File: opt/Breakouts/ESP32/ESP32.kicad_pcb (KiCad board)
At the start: 2 copper layers, 23.4 x 25.9 mm, 3 parts, among them J1 LEFT, J2 RIGHT, U2 ESP32-S3-MINI-1

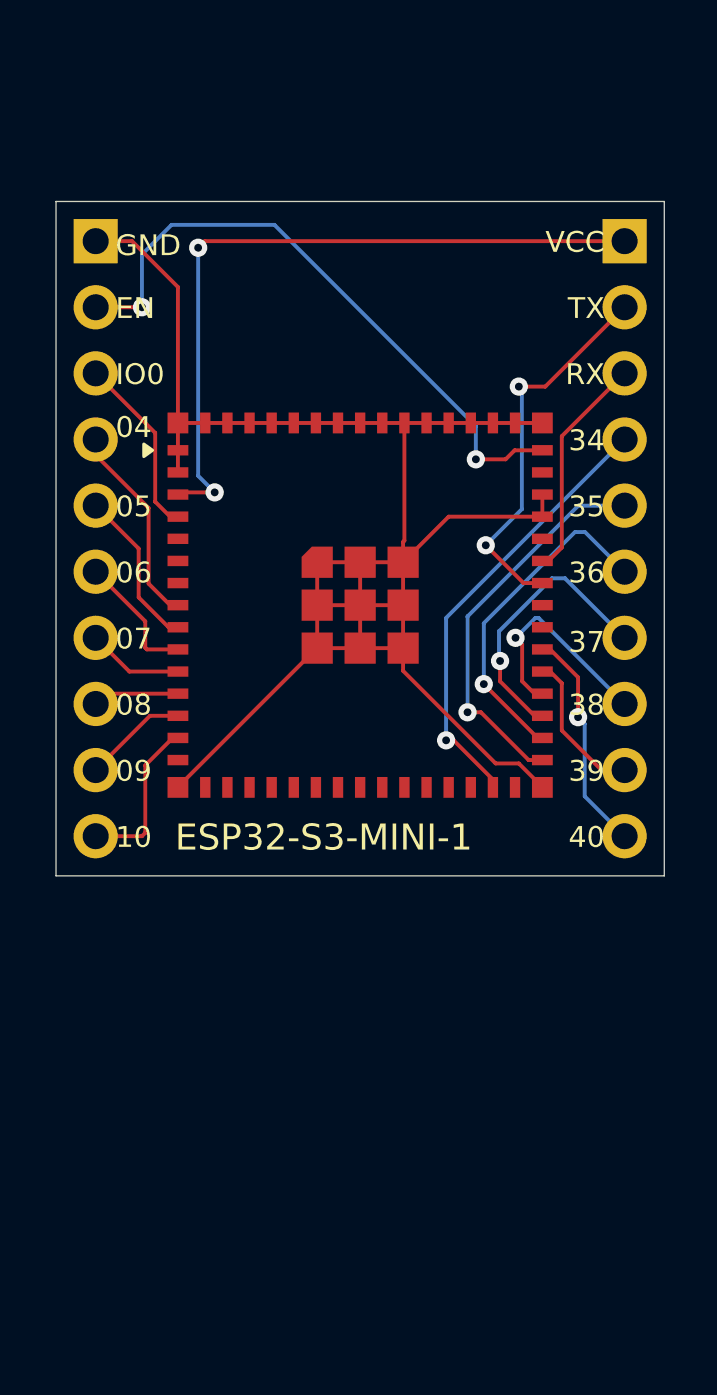
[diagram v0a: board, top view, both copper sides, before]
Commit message: breakouts: Merge ESP32 and PT8211 pcbs
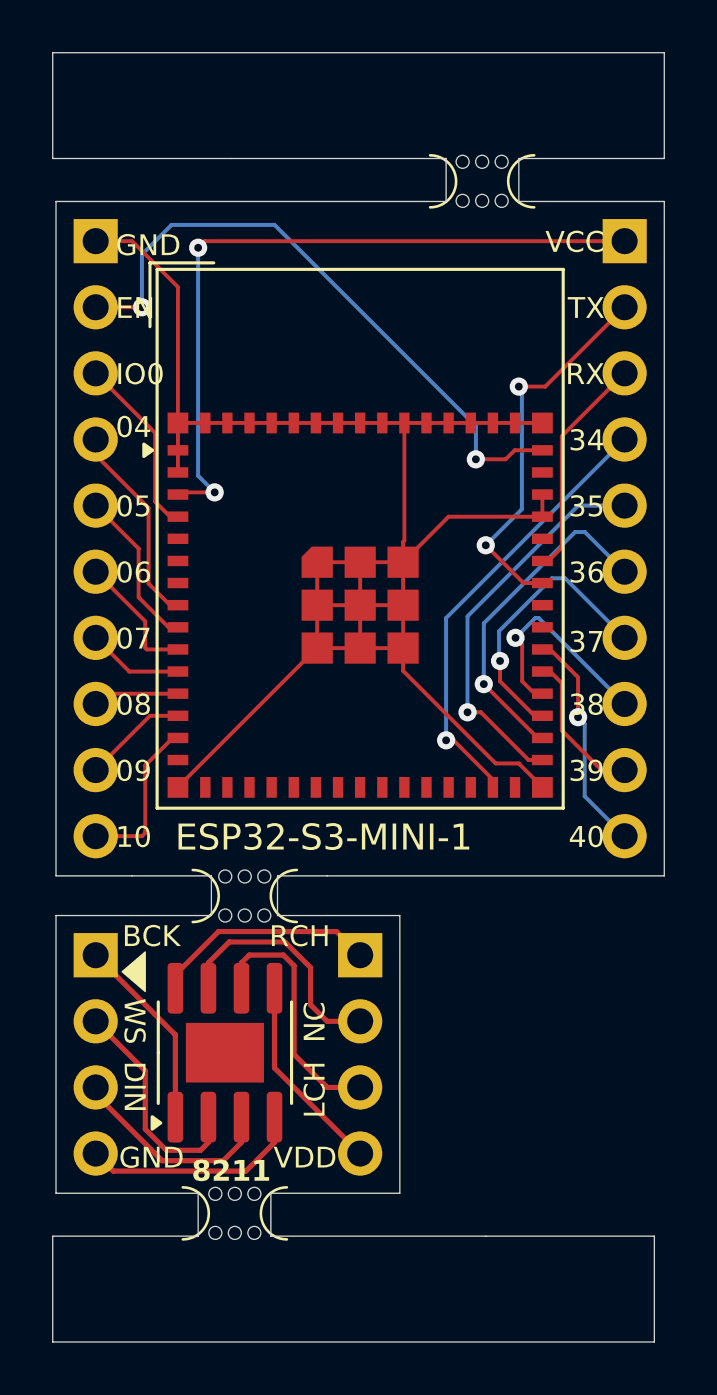
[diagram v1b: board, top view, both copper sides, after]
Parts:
- added J3: Conn_01x04_Pin, Connector_PinSocket_2.54mm:PinSocket_1x04_P2.54mm_Vertical, B.Cu at (152.4, 141.7)
- added J4: Conn_01x04_Pin, Connector_PinSocket_2.54mm:PinSocket_1x04_P2.54mm_Vertical, B.Cu at (162.6, 141.7)
- added U2: ~, Package_SO:SOIC-8-1EP_3.9x4.9mm_P1.27mm_EP2.29x3mm, F.Cu at (157.4, 145.5)
- added mouse-bite-2mm-slot: VAL**, BreadModular_Panalize:mouse-bite-2mm-slot, F.Cu at (157.7, 151.7)
- added mouse-bite-2mm-slot: VAL**, BreadModular_Panalize:mouse-bite-2mm-slot, F.Cu at (167.2, 112.0)
- added mouse-bite-2mm-slot: VAL**, BreadModular_Panalize:mouse-bite-2mm-slot, F.Cu at (158.1, 139.5)
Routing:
- net Net-(J4-Pin_3): track 0.00 -> 9.76 mm
- net Net-(J4-Pin_2): track 0.00 -> 9.24 mm
- net Net-(J3-Pin_2): track 0.00 -> 8.79 mm
- net Net-(J4-Pin_1): track 0.00 -> 8.68 mm
- net Net-(J3-Pin_4): track 0.00 -> 8.58 mm
- net Net-(J3-Pin_3): track 0.00 -> 8.18 mm
- net Net-(J4-Pin_4): track 0.00 -> 7.71 mm
- net Net-(J3-Pin_1): track 0.00 -> 7.49 mm
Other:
- board size 23.4 x 25.9 mm -> 23.5 x 49.5 mm
- board text added: "8211"
- board text added: "BCK"
- board text added: "DIN"
- board text added: "LCH"
- board text added: "NC"
- board text added: "RCH"
- board text added: "VDD"
- board text added: "WS"
